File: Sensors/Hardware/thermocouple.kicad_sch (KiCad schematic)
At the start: 8 parts, among them U4 MAX31856

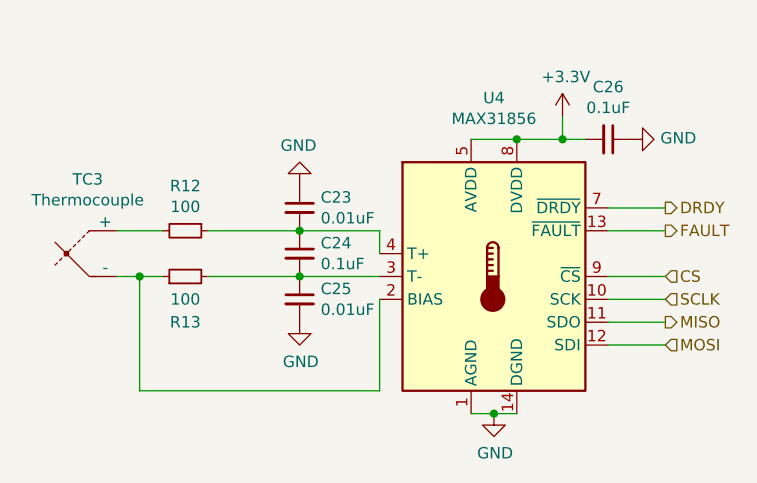
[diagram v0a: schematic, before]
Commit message: ADC connections and KiCAD version update
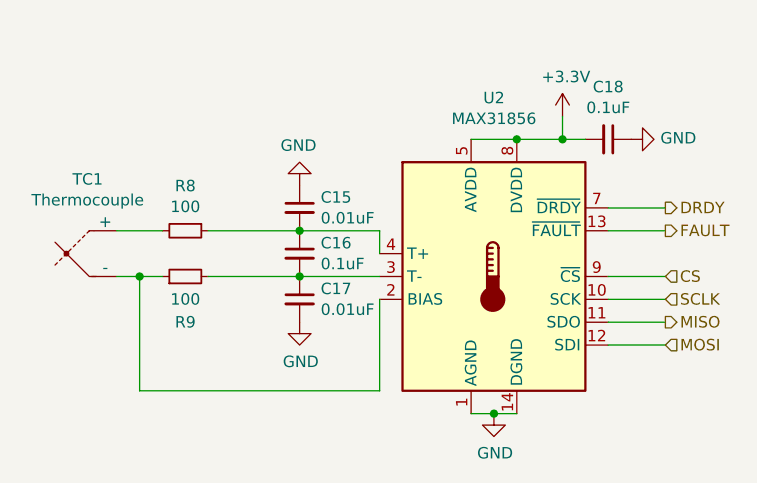
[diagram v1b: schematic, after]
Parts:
- renumbered C23 to C15, C24 to C16, C25 to C17, C26 to C18, R12 to R8, R13 to R9, TC3 to TC1, U4 to U2

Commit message: Schematic update
unfinished
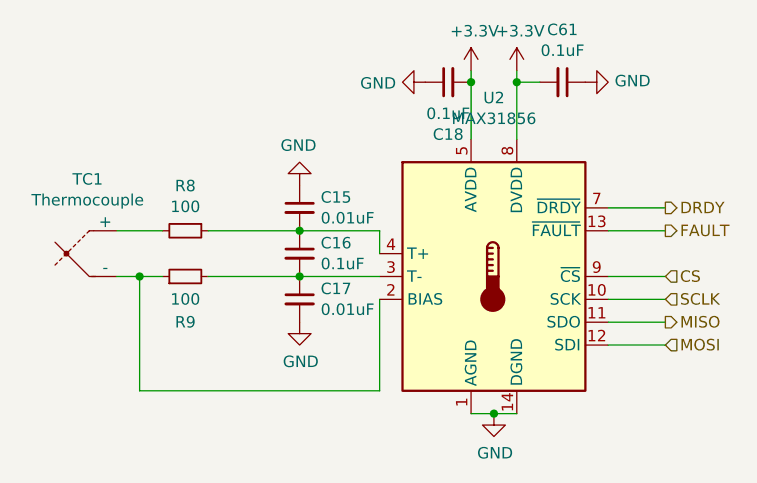
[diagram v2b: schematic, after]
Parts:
- added C61: 0.1uF, Capacitor_SMD:C_0402_1005Metric, symbol Device:C_Small
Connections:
- net +3V3: now also C61.2
- net GND: now also C61.1
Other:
- moved on the sheet: C18
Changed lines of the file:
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@@
 (kicad_sch (version 20230121) (generator eeschema)
   (paper "A4")
-  (junction (at 97.79 58.42) (diameter 0) (color 0 0 0 0)
+  (junction (at 92.71 52.07) (diameter 0) (color 0 0 0 0)
   )
   (junction (at 73.66 73.66) (diameter 0) (color 0 0 0 0)
@@
   (junction (at 95.25 88.9) (diameter 0) (color 0 0 0 0)
   )
+  (junction (at 97.79 52.07) (diameter 0) (color 0 0 0 0)
+  )
   (junction (at 73.66 68.58) (diameter 0) (color 0 0 0 0)
   )
-  (junction (at 102.87 58.42) (diameter 0) (color 0 0 0 0)
-  )
   (wire (pts (xy 55.88 73.66) (xy 58.42 73.66))
     (stroke (width 0) (type default))
@@
     (stroke (width 0) (type default))
   )
+  (wire (pts (xy 97.79 52.07) (xy 97.79 50.8))
+    (stroke (width 0) (type default))
+  )
   (wire (pts (xy 97.79 88.9) (xy 95.25 88.9))
     (stroke (width 0) (type default))
   )
+  (wire (pts (xy 92.71 52.07) (xy 92.71 58.42))
+    (stroke (width 0) (type default))
+  )
   (wire (pts (xy 63.5 73.66) (xy 73.66 73.66))
     (stroke (width 0) (type default))
   )
-  (wire (pts (xy 97.79 58.42) (xy 102.87 58.42))
-    (stroke (width 0) (type default))
-  )
   (wire (pts (xy 114.3 78.74) (xy 107.95 78.74))
     (stroke (width 0) (type default))
   )
-  (wire (pts (xy 102.87 55.88) (xy 102.87 58.42))
+  (wire (pts (xy 92.71 52.07) (xy 92.71 50.8))
+    (stroke (width 0) (type default))
+  )
+  (wire (pts (xy 97.79 52.07) (xy 97.79 58.42))
     (stroke (width 0) (type default))
   )
@@
     (stroke (width 0) (type default))
   )
-  (wire (pts (xy 102.87 58.42) (xy 105.41 58.42))
+  (wire (pts (xy 100.33 52.07) (xy 97.79 52.07))
     (stroke (width 0) (type default))
   )
@@
   )
   (wire (pts (xy 82.55 86.36) (xy 55.88 86.36))
-    (stroke (width 0) (type default))
-  )
-  (wire (pts (xy 92.71 58.42) (xy 97.79 58.42))
     (stroke (width 0) (type default))
   )
@@
     )
   )
-  (symbol (lib_id "analogue-cache:+3.3V") (at 102.87 55.88 0) (unit 1)
-    (in_bom yes) (on_board yes) (dnp no)
-    (property "Reference" "#PWR030" (at 102.87 59.69 0)
-      (effects (font (size 1.27 1.27)) hide)
-    )
-    (property "Value" "+3.3V" (at 103.251 51.4858 0)
-      (effects (font (size 1.27 1.27)))
-    )
-    (property "Footprint" "" (at 102.87 55.88 0)
-      (effects (font (size 1.27 1.27)) hide)
-    )
-    (property "Datasheet" "" (at 102.87 55.88 0)
+  (symbol (lib_id "analogue-cache:+3.3V") (at 92.71 50.8 0) (unit 1)
+    (in_bom yes) (on_board yes) (dnp no)
+    (property "Reference" "#PWR030" (at 92.71 54.61 0)
+      (effects (font (size 1.27 1.27)) hide)
+    )
+    (property "Value" "+3.3V" (at 93.091 46.4058 0)
+      (effects (font (size 1.27 1.27)))
+    )
+    (property "Footprint" "" (at 92.71 50.8 0)
+      (effects (font (size 1.27 1.27)) hide)
+    )
+    (property "Datasheet" "" (at 92.71 50.8 0)
       (effects (font (size 1.27 1.27)) hide)
     )
@@
     )
   )
-  (symbol (lib_id "Device:C_Small") (at 107.95 58.42 270) (unit 1)
-    (in_bom yes) (on_board yes) (dnp no)
-    (property "Reference" "C18" (at 107.95 52.6034 90)
-      (effects (font (size 1.27 1.27)))
-    )
-    (property "Value" "0.1uF" (at 107.95 54.9148 90)
-      (effects (font (size 1.27 1.27)))
-    )
-    (property "Footprint" "Capacitor_SMD:C_0402_1005Metric" (at 107.95 58.42 0)
-      (effects (font (size 1.27 1.27)) hide)
-    )
-    (property "Datasheet" "~" (at 107.95 58.42 0)
+  (symbol (lib_id "Device:C_Small") (at 90.17 52.07 90) (unit 1)
+    (in_bom yes) (on_board yes) (dnp no)
+    (property "Reference" "C18" (at 90.17 57.8866 90)
+      (effects (font (size 1.27 1.27)))
+    )
+    (property "Value" "0.1uF" (at 90.17 55.5752 90)
+      (effects (font (size 1.27 1.27)))
+    )
+    (property "Footprint" "Capacitor_SMD:C_0402_1005Metric" (at 90.17 52.07 0)
+      (effects (font (size 1.27 1.27)) hide)
+    )
+    (property "Datasheet" "~" (at 90.17 52.07 0)
       (effects (font (size 1.27 1.27)) hide)
     )
@@
     )
   )
-  (symbol (lib_id "power:GND") (at 110.49 58.42 90) (unit 1)
-    (in_bom yes) (on_board yes) (dnp no)
-    (property "Reference" "#PWR031" (at 116.84 58.42 0)
-      (effects (font (size 1.27 1.27)) hide)
-    )
-    (property "Value" "GND" (at 113.7412 58.293 90)
+  (symbol (lib_id "power:GND") (at 87.63 52.07 270) (unit 1)
+    (in_bom yes) (on_board yes) (dnp no)
+    (property "Reference" "#PWR031" (at 81.28 52.07 0)
+      (effects (font (size 1.27 1.27)) hide)
+    )
+    (property "Value" "GND" (at 84.3788 52.197 90)
       (effects (font (size 1.27 1.27)) (justify right))
     )
-    (property "Footprint" "" (at 110.49 58.42 0)
-      (effects (font (size 1.27 1.27)) hide)
-    )
-    (property "Datasheet" "" (at 110.49 58.42 0)
+    (property "Footprint" "" (at 87.63 52.07 0)
+      (effects (font (size 1.27 1.27)) hide)
+    )
+    (property "Datasheet" "" (at 87.63 52.07 0)
       (effects (font (size 1.27 1.27)) hide)
     )
@@
         )
       )
+    )
+  )
+  (symbol (lib_id "power:GND") (at 105.41 52.07 90) (unit 1)
+    (in_bom yes) (on_board yes) (dnp no)
+    (property "Reference" "#PWR0172" (at 111.76 52.07 0)
+      (effects (font (size 1.27 1.27)) hide)
+    )
+    (property "Value" "GND" (at 108.6612 51.943 90)
+      (effects (font (size 1.27 1.27)) (justify right))
+    )
+    (property "Footprint" "" (at 105.41 52.07 0)
+      (effects (font (size 1.27 1.27)) hide)
+    )
+    (property "Datasheet" "" (at 105.41 52.07 0)
+      (effects (font (size 1.27 1.27)) hide)
+    )
+    (pin "1")
+    (instances
+      (project "sensorboard"
+        (path "/26801cfb-b53b-4a6a-a2f4-5f4986565765/00000000-0000-0000-0000-000061cb93b1"
+          (reference "#PWR0172") (unit 1)
+        )
+        (path "/26801cfb-b53b-4a6a-a2f4-5f4986565765/00000000-0000-0000-0000-000061d785e6"
+          (reference "#PWR0174") (unit 1)
+        )
+        (path "/26801cfb-b53b-4a6a-a2f4-5f4986565765/00000000-0000-0000-0000-000061d7d3f0"
+          (reference "#PWR0178") (unit 1)
+        )
+        (path "/26801cfb-b53b-4a6a-a2f4-5f4986565765/00000000-0000-0000-0000-000061d8261a"
+          (reference "#PWR0176") (unit 1)
+        )
+      )
+    )
+  )
+  (symbol (lib_id "analogue-cache:+3.3V") (at 97.79 50.8 0) (unit 1)
+    (in_bom yes) (on_board yes) (dnp no)
+    (property "Reference" "#PWR0171" (at 97.79 54.61 0)
+      (effects (font (size 1.27 1.27)) hide)
+    )
+    (property "Value" "+3.3V" (at 98.171 46.4058 0)
+      (effects (font (size 1.27 1.27)))
+    )
+    (property "Footprint" "" (at 97.79 50.8 0)
+      (effects (font (size 1.27 1.27)) hide)
+    )
+    (property "Datasheet" "" (at 97.79 50.8 0)
+      (effects (font (size 1.27 1.27)) hide)
+    )
+    (pin "1")
+    (instances
+      (project "sensorboard"
+        (path "/26801cfb-b53b-4a6a-a2f4-5f4986565765/00000000-0000-0000-0000-000061cb93b1"
+          (reference "#PWR0171") (unit 1)
+        )
+        (path "/26801cfb-b53b-4a6a-a2f4-5f4986565765/00000000-0000-0000-0000-000061d785e6"
+          (reference "#PWR0173") (unit 1)
+        )
+        (path "/26801cfb-b53b-4a6a-a2f4-5f4986565765/00000000-0000-0000-0000-000061d7d3f0"
+          (reference "#PWR0177") (unit 1)
+        )
+        (path "/26801cfb-b53b-4a6a-a2f4-5f4986565765/00000000-0000-0000-0000-000061d8261a"
+          (reference "#PWR0175") (unit 1)
+        )
+      )
+    )
+  )
+  (symbol (lib_id "Device:C_Small") (at 102.87 52.07 270) (unit 1)
+    (in_bom yes) (on_board yes) (dnp no)
+    (property "Reference" "C61" (at 102.87 46.2534 90)
+      (effects (font (size 1.27 1.27)))
+    )
+    (property "Value" "0.1uF" (at 102.87 48.5648 90)
+      (effects (font (size 1.27 1.27)))
+    )
+    (property "Footprint" "Capacitor_SMD:C_0402_1005Metric" (at 102.87 52.07 0)
+      (effects (font (size 1.27 1.27)) hide)
+    )
+    (property "Datasheet" "~" (at 102.87 52.07 0)
+      (effects (font (size 1.27 1.27)) hide)
+    )
+    (pin "1")
+    (pin "2")
+    (instances
+      (project "sensorboard"
+        (path "/26801cfb-b53b-4a6a-a2f4-5f4986565765/00000000-0000-0000-0000-000061cb93b1"
+          (reference "C61") (unit 1)
+        )
+        (path "/26801cfb-b53b-4a6a-a2f4-5f4986565765/00000000-0000-0000-0000-000061d785e6"
+          (reference "C62") (unit 1)
+        )
+        (path "/26801cfb-b53b-4a6a-a2f4-5f4986565765/00000000-0000-0000-0000-000061d7d3f0"
+          (reference "C86") (unit 1)
+        )
+        (path "/26801cfb-b53b-4a6a-a2f4-5f4986565765/00000000-0000-0000-0000-000061d8261a"
+          (reference "C85") (unit 1)
+        )
+      )

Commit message: switched tc references
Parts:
- renumbered TC1 to TC2
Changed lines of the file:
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@@
   (symbol (lib_id "Device:Thermocouple") (at 50.8 71.12 0) (unit 1)
     (in_bom yes) (on_board yes) (dnp no)
-    (property "Reference" "TC1" (at 50.1142 62.865 0)
+    (property "Reference" "TC2" (at 50.1142 62.865 0)
       (effects (font (size 1.27 1.27)))
     )
@@
       (project "sensorboard"
         (path "/26801cfb-b53b-4a6a-a2f4-5f4986565765/00000000-0000-0000-0000-000061cb93b1"
-          (reference "TC1") (unit 1)
+          (reference "TC2") (unit 1)
         )
         (path "/26801cfb-b53b-4a6a-a2f4-5f4986565765/00000000-0000-0000-0000-000061d785e6"
-          (reference "TC2") (unit 1)
+          (reference "TC3") (unit 1)
         )
         (path "/26801cfb-b53b-4a6a-a2f4-5f4986565765/00000000-0000-0000-0000-000061d7d3f0"
@@
         )
         (path "/26801cfb-b53b-4a6a-a2f4-5f4986565765/00000000-0000-0000-0000-000061d8261a"
-          (reference "TC3") (unit 1)
+          (reference "TC1") (unit 1)
         )
       )
